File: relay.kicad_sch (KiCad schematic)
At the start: 3 parts, among them K1 SANYOU_SRD_Form_C, Q1 BCP56

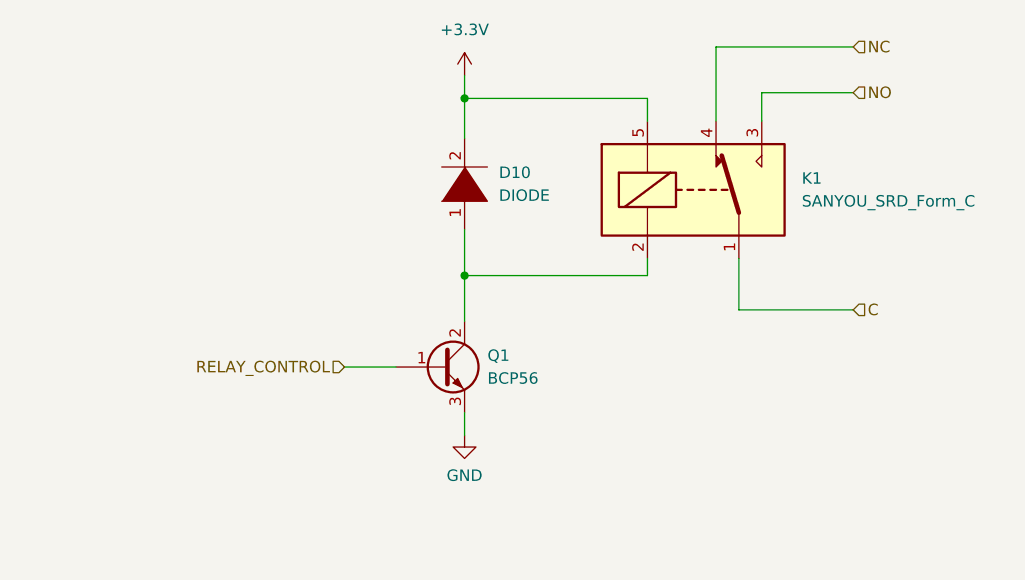
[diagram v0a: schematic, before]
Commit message: feat: add more LCSC symbols
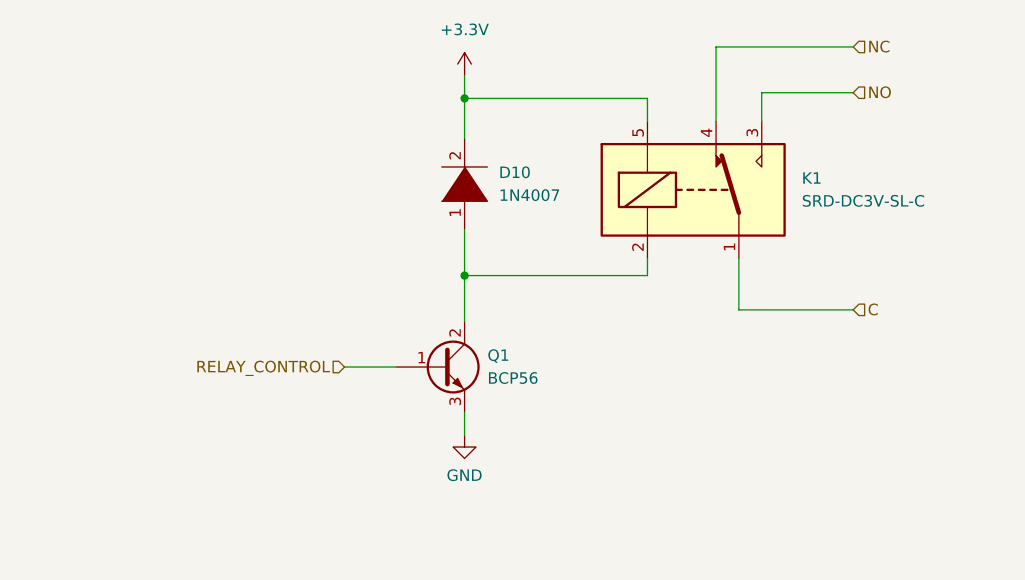
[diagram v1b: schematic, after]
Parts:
- D10: value DIODE -> 1N4007; footprint (none) -> Diode_SMD:D_SMA_Handsoldering; LCSC (none) -> C727081
- K1: value SANYOU_SRD_Form_C -> SRD-DC3V-SL-C; LCSC (none) -> C688864
- Q1: LCSC (none) -> C549595
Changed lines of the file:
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@@
       (effects (font (size 1.27 1.27)) (justify left))
     )
-    (property "Value" "SANYOU_SRD_Form_C" (id 1) (at 172.085 87.6299 0)
+    (property "Value" "SRD-DC3V-SL-C" (id 1) (at 172.085 87.6299 0)
       (effects (font (size 1.27 1.27)) (justify left))
     )
@@
       (effects (font (size 1.27 1.27)) (justify left) hide)
     )
-    (property "Datasheet" "http://www.sanyourelay.ca/public/products/pdf/SRD.pdf" (id 3) (at 160.02 86.36 0)
+    (property "Datasheet" "https://datasheet.lcsc.com/lcsc/2006281940_Ningbo-Songle-Relay-SRD-DC3V-SL-C_C688864.pdf" (id 3) (at 160.02 86.36 0)
+      (effects (font (size 1.27 1.27)) hide)
+    )
+    (property "LCSC" "C688864" (id 4) (at 160.02 86.36 0)
       (effects (font (size 1.27 1.27)) hide)
     )
@@
       (effects (font (size 1.27 1.27) italic) (justify left) hide)
     )
-    (property "Datasheet" "http://cache.nxp.com/documents/data_sheet/BCP56_BCX56_BC56PA.pdf?pspll=1" (id 3) (at 132.08 106.045 0)
+    (property "Datasheet" "https://datasheet.lcsc.com/lcsc/2007030435_Nexperia-BCP56F_C549595.pdf" (id 3) (at 132.08 106.045 0)
       (effects (font (size 1.27 1.27)) (justify left) hide)
+    )
+    (property "LCSC" "C549595" (id 4) (at 132.08 106.045 0)
+      (effects (font (size 1.27 1.27)) hide)
     )
     (pin "1")
@@
       (effects (font (size 1.27 1.27)) (justify right))
     )
-    (property "Value" "DIODE" (id 1) (at 138.43 86.9949 90)
+    (property "Value" "1N4007" (id 1) (at 138.43 86.9949 90)
       (effects (font (size 1.27 1.27)) (justify right))
     )
-    (property "Footprint" "" (id 2) (at 134.62 85.725 0)
+    (property "Footprint" "Diode_SMD:D_SMA_Handsoldering" (id 2) (at 134.62 85.725 0)
       (effects (font (size 1.27 1.27)) hide)
     )
-    (property "Datasheet" "~" (id 3) (at 134.62 85.725 0)
+    (property "Datasheet" "https://datasheet.lcsc.com/lcsc/2008281133_TWGMC-1N4007_C727081.pdf" (id 3) (at 134.62 85.725 0)
       (effects (font (size 1.27 1.27)) hide)
     )
+    (property "LCSC" "C727081" (id 4) (at 134.62 85.725 90)
+      (effects (font (size 1.27 1.27)) hide)
+    )

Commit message: Finish layout
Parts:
- added R32: R, Resistor_SMD:R_0603_1608Metric_Pad0.98x0.95mm_HandSolder, symbol Device:R
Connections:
- net RELAY_CONTROL: now also R32.1; no longer Q1.1 (B)
- new net: Q1.1 (B), R32.2
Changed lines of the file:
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@@
+    (stroke (width 0) (type default) (color 0 0 0 0))
+  )
+  (wire (pts (xy 106.045 106.045) (xy 113.665 106.045))
     (stroke (width 0) (type default) (color 0 0 0 0))
   )
@@
     (effects (font (size 1.27 1.27)) (justify left))
   )
-  (hierarchical_label "RELAY_CONTROL" (shape input) (at 121.285 106.045 180)
+  (hierarchical_label "RELAY_CONTROL" (shape input) (at 106.045 106.045 180)
     (effects (font (size 1.27 1.27)) (justify right))
   )
@@
       (effects (font (size 1.27 1.27)) hide)
     )
+    (pin "1")
+    (pin "2")
+  )
+  (symbol (lib_id "Device:R") (at 117.475 106.045 90) (unit 1)
+    (in_bom yes) (on_board yes) (fields_autoplaced)
+    (property "Reference" "R32" (id 0) (at 117.475 99.695 90))
+    (property "Value" "R" (id 1) (at 117.475 102.235 90))
+    (property "Footprint" "Resistor_SMD:R_0603_1608Metric_Pad0.98x0.95mm_HandSolder" (id 2) (at 117.475 107.823 90)
+      (effects (font (size 1.27 1.27)) hide)
+    )
+    (property "Datasheet" "~" (id 3) (at 117.475 106.045 0)
+      (effects (font (size 1.27 1.27)) hide)
+    )

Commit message: DO the bulk of rev 1.2 layout
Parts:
- removed D10: 1N4007, Diode_SMD:D_SMA_Handsoldering, symbol pspice:DIODE
- removed Q1: BCP56, Package_TO_SOT_SMD:SOT-223-3_TabPin2, symbol Transistor_BJT:BCP56
- added D10: 1N4007, Diode_SMD:D_SMA_Handsoldering, symbol Diode:1N4007
- added Q1: DMG2302U, Package_TO_SOT_SMD:SOT-23, symbol Transistor_FET:DMG2302U
- added R37: 100K 1%, Resistor_SMD:R_0603_1608Metric_Pad0.98x0.95mm_HandSolder, symbol Device:R
- R32: value R -> 1k
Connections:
- net +3.3V: now also K1.2, D10.1 (K); no longer K1.5
- net GND: now also Q1.2 (S), R37.2
- net RELAY_CONTROL: now also R37.1
- net at R32.2: now also Q1.1 (G)
- new net: D10.2 (A), K1.5, Q1.3 (D)
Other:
- moved on the sheet: R32

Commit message: BOM updates
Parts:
- D10: LCSC (none) -> C7528875
- Q1: LCSC (none) -> C460977
- R32: LCSC (none) -> C22548
- R37: LCSC (none) -> C2906980

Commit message: Zamkonator rev 1.3
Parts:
- renumbered D10 to D20, R37 to R43, R32 to R44
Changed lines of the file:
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@@
 		(dnp no)
 		(fields_autoplaced yes)
-		(property "Reference" "R37"
+		(property "Reference" "R43"
 			(at 110.49 113.0299 0)
 			(show_name no)
@@
 			(project "Zamkonator"
 				(path "/727d6c0a-a0ef-4feb-9656-3db3cb90564a/f0d3712c-d6bb-4e32-851a-ff1f073efd27"
-					(reference "R37")
+					(reference "R43")
 					(unit 1)
 				)
@@
 		(dnp no)
 		(fields_autoplaced yes)
-		(property "Reference" "#PWR066"
+		(property "Reference" "#PWR0109"
 			(at 134.62 124.46 0)
 			(hide yes)
@@
 			(project "Zamkonator"
 				(path "/727d6c0a-a0ef-4feb-9656-3db3cb90564a/f0d3712c-d6bb-4e32-851a-ff1f073efd27"
-					(reference "#PWR066")
+					(reference "#PWR0109")
 					(unit 1)
 				)
@@
 		(dnp no)
 		(fields_autoplaced yes)
-		(property "Reference" "#PWR065"
+		(property "Reference" "#PWR0108"
 			(at 134.62 77.47 0)
 			(hide yes)
@@
 			(project "Zamkonator"
 				(path "/727d6c0a-a0ef-4feb-9656-3db3cb90564a/f0d3712c-d6bb-4e32-851a-ff1f073efd27"
-					(reference "#PWR065")
+					(reference "#PWR0108")
 					(unit 1)
 				)
@@
 		(dnp no)
 		(fields_autoplaced yes)
-		(property "Reference" "D10"
+		(property "Reference" "D20"
 			(at 137.16 83.8199 90)
 			(show_name no)
@@
 			(project "Zamkonator"
 				(path "/727d6c0a-a0ef-4feb-9656-3db3cb90564a/f0d3712c-d6bb-4e32-851a-ff1f073efd27"
-					(reference "D10")
+					(reference "D20")
 					(unit 1)
 				)
@@
 		(dnp no)
 		(fields_autoplaced yes)
-		(property "Reference" "R32"
+		(property "Reference" "R44"
 			(at 115.57 100.33 90)
 			(show_name no)
@@
 			(project "Zamkonator"
 				(path "/727d6c0a-a0ef-4feb-9656-3db3cb90564a/f0d3712c-d6bb-4e32-851a-ff1f073efd27"
-					(reference "R32")
+					(reference "R44")
 					(unit 1)
 				)
@@
 		(dnp no)
 		(fields_autoplaced yes)
-		(property "Reference" "#PWR057"
+		(property "Reference" "#PWR0107"
 			(at 107.95 128.27 0)
 			(hide yes)
@@
 			(project "Zamkonator"
 				(path "/727d6c0a-a0ef-4feb-9656-3db3cb90564a/f0d3712c-d6bb-4e32-851a-ff1f073efd27"
-					(reference "#PWR057")
+					(reference "#PWR0107")
 					(unit 1)
 				)
